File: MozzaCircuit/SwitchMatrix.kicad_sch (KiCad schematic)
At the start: 94 parts, among them SW13 SW_ChocV2_rev, SW14 SW_ChocV2_rev, SW15 SW_ChocV2_rev, SW21 SW_ChocV2_rev, SW22 SW_ChocV2_rev, SW23 SW_ChocV2_rev, SW24 SW_ChocV2_rev, SW25 SW_ChocV2_rev, SW31 SW_ChocV2_rev, SW32 SW_ChocV2_rev, SW33 SW_ChocV2_rev, SW34 SW_ChocV2_rev, SW35 SW_ChocV2_rev, SW41 SW_ChocV2_rev, SW42 SW_ChocV2_rev, SW43 SW_ChocV2_rev, SW44 SW_ChocV2_rev, SW51 SW_ChocV2_rev, SW52 SW_ChocV2_rev, SW53 SW_ChocV2_rev, SW54 SW_ChocV2_rev, SW61 SW_ChocV2_rev, SW62 SW_ChocV2_rev, SW63 SW_ChocV2_rev, SW64 SW_ChocV2_rev, SW71 SW_ChocV2_rev, SW72 SW_ChocV2_rev, SW73 SW_ChocV2_rev, SW82 SW_ChocV2_rev, SW83 SW_ChocV2_rev, SW84 SW_ChocV2_rev

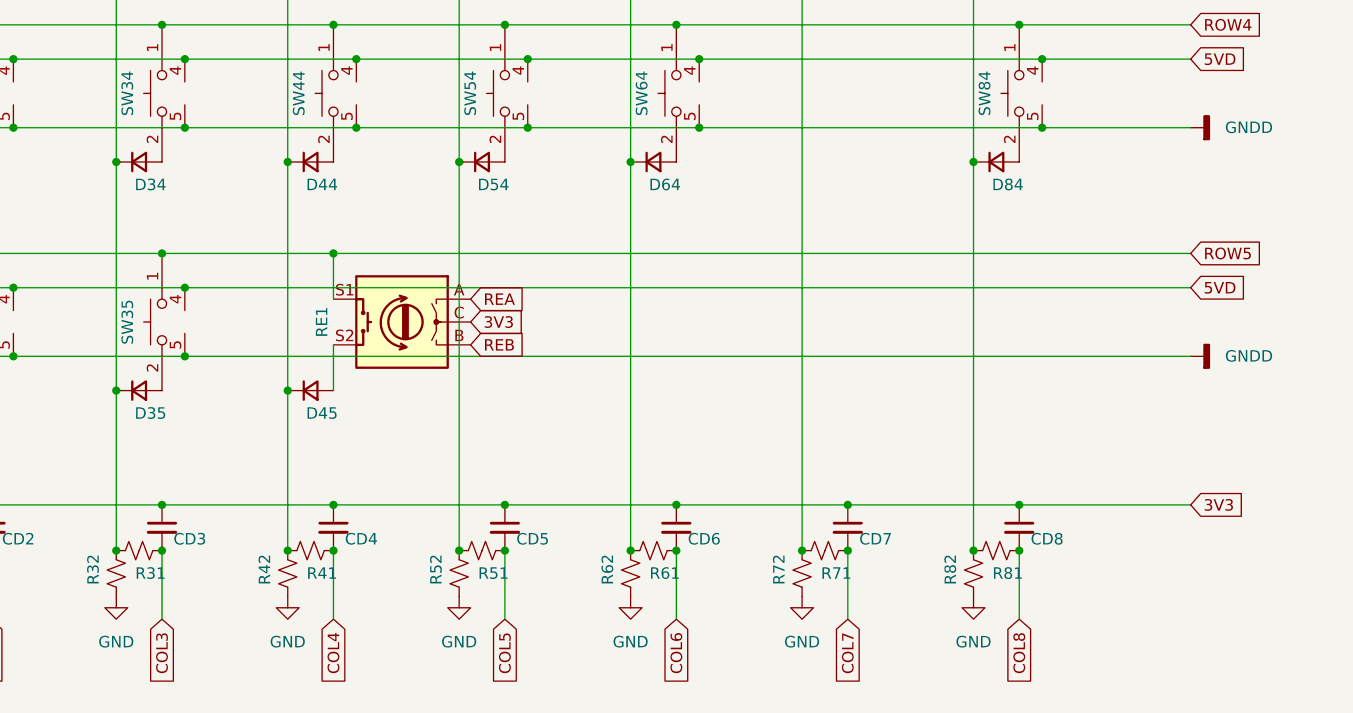
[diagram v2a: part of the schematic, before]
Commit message: rotate rot_enc
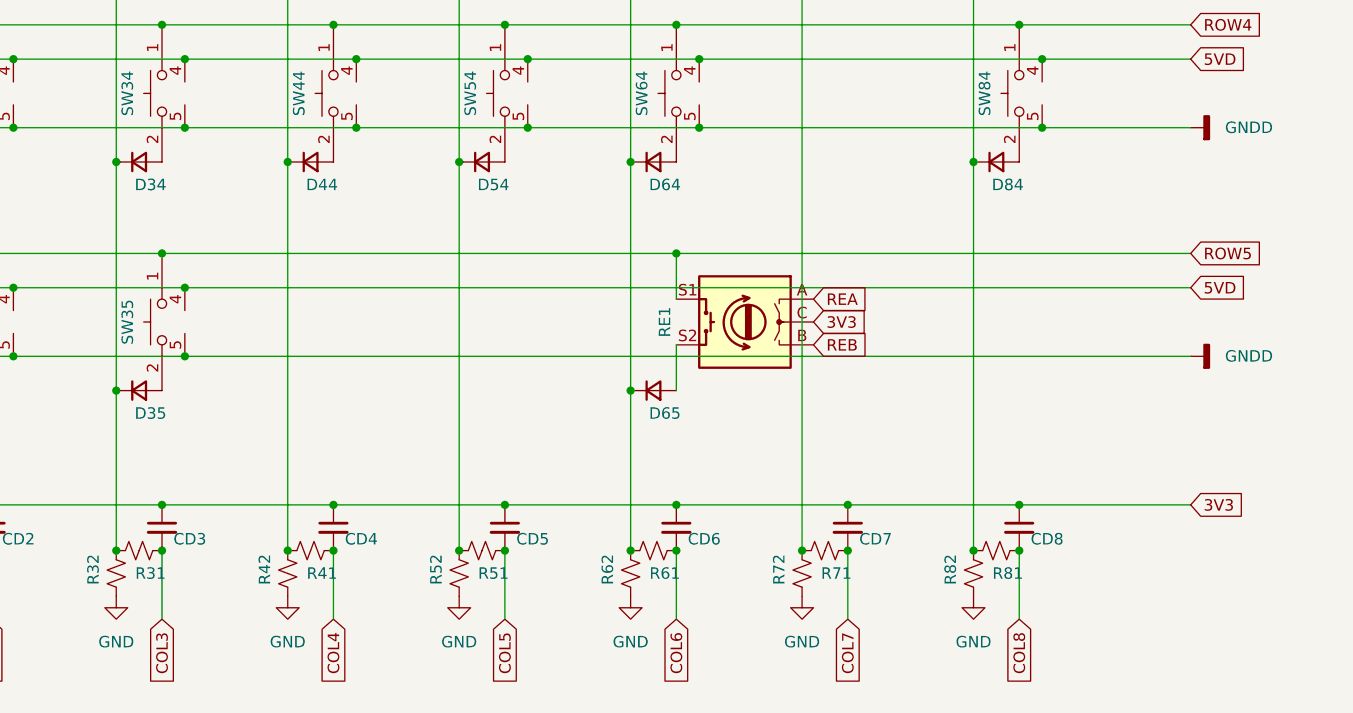
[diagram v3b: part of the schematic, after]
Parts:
- renumbered D45 to D65
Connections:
- net at D41.1 (K), D42.1 (K), D43.1 (K)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: no longer D65.1 (K)
- net at D61.1 (K), D62.1 (K), D63.1 (K)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: now also D65.1 (K)
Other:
- moved on the sheet: D65, RE1
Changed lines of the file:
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@@
   (junction (at 72.39 113.03) (diameter 0) (color 0 0 0 0)
   )
-  (junction (at 88.9 127) (diameter 0) (color 0 0 0 0)
-  )
   (junction (at 69.85 76.2) (diameter 0) (color 0 0 0 0)
   )
@@
   (junction (at 50.8 101.6) (diameter 0) (color 0 0 0 0)
   )
+  (junction (at 121.92 142.24) (diameter 0) (color 0 0 0 0)
+  )
   (junction (at 72.39 54.61) (diameter 0) (color 0 0 0 0)
   )
@@
   (junction (at 53.34 80.01) (diameter 0) (color 0 0 0 0)
   )
+  (junction (at 127 127) (diameter 0) (color 0 0 0 0)
+  )
   (junction (at 53.34 87.63) (diameter 0) (color 0 0 0 0)
   )
@@
   (junction (at 88.9 25.4) (diameter 0) (color 0 0 0 0)
   )
-  (junction (at 83.82 142.24) (diameter 0) (color 0 0 0 0)
-  )
   (junction (at 148.59 62.23) (diameter 0) (color 0 0 0 0)
   )
@@
     (stroke (width 0) (type default) (color 0 0 0 0))
   )
-  (wire (pts (xy 83.82 116.84) (xy 83.82 142.24))
-    (stroke (width 0) (type default) (color 0 0 0 0))
-  )
   (wire (pts (xy 148.59 54.61) (xy 167.64 54.61))
     (stroke (width 0) (type default) (color 0 0 0 0))
@@
     (stroke (width 0) (type default) (color 0 0 0 0))
   )
-  (wire (pts (xy 88.9 137.16) (xy 88.9 142.24))
+  (wire (pts (xy 127 137.16) (xy 127 142.24))
     (stroke (width 0) (type default) (color 0 0 0 0))
   )
@@
     (stroke (width 0) (type default) (color 0 0 0 0))
   )
-  (wire (pts (xy 88.9 127) (xy 184.15 127))
-    (stroke (width 0) (type default) (color 0 0 0 0))
-  )
   (wire (pts (xy 72.39 80.01) (xy 91.44 80.01))
     (stroke (width 0) (type default) (color 0 0 0 0))
@@
     (stroke (width 0) (type default) (color 0 0 0 0))
   )
-  (wire (pts (xy 83.82 142.24) (xy 83.82 160.02))
+  (wire (pts (xy 83.82 116.84) (xy 83.82 160.02))
     (stroke (width 0) (type default) (color 0 0 0 0))
   )
@@
     (stroke (width 0) (type default) (color 0 0 0 0))
   )
+  (wire (pts (xy 127 127) (xy 184.15 127))
+    (stroke (width 0) (type default) (color 0 0 0 0))
+  )
   (wire (pts (xy 140.97 66.04) (xy 140.97 91.44))
     (stroke (width 0) (type default) (color 0 0 0 0))
@@
     (stroke (width 0) (type default) (color 0 0 0 0))
   )
+  (wire (pts (xy 121.92 142.24) (xy 121.92 160.02))
+    (stroke (width 0) (type default) (color 0 0 0 0))
+  )
   (wire (pts (xy 146.05 154.94) (xy 165.1 154.94))
     (stroke (width 0) (type default) (color 0 0 0 0))
@@
     (stroke (width 0) (type default) (color 0 0 0 0))
   )
-  (wire (pts (xy 121.92 116.84) (xy 121.92 160.02))
+  (wire (pts (xy 121.92 116.84) (xy 121.92 142.24))
     (stroke (width 0) (type default) (color 0 0 0 0))
   )
@@
     (stroke (width 0) (type default) (color 0 0 0 0))
   )
-  (wire (pts (xy 88.9 127) (xy 88.9 132.08))
+  (wire (pts (xy 127 127) (xy 127 132.08))
     (stroke (width 0) (type default) (color 0 0 0 0))
   )
@@
     (stroke (width 0) (type default) (color 0 0 0 0))
   )
-  (wire (pts (xy 69.85 127) (xy 88.9 127))
+  (wire (pts (xy 69.85 127) (xy 127 127))
     (stroke (width 0) (type default) (color 0 0 0 0))
   )
@@
     )
   )
-  (global_label "3V3" (shape input) (at 104.14 134.62 0) (fields_autoplaced)
+  (global_label "3V3" (shape input) (at 142.24 134.62 0) (fields_autoplaced)
     (effects (font (size 1.27 1.27)) (justify left))
-    (property "Intersheet References" "${INTERSHEET_REFS}" (id 0) (at 110.0607 134.5406 0)
-      (effects (font (size 1.27 1.27)) (justify left) hide)
-    )
-  )
-  (global_label "REA" (shape input) (at 104.14 132.08 0) (fields_autoplaced)
+    (property "Intersheet References" "${INTERSHEET_REFS}" (id 0) (at 148.1607 134.5406 0)
+      (effects (font (size 1.27 1.27)) (justify left) hide)
+    )
+  )
+  (global_label "REA" (shape input) (at 142.24 132.08 0) (fields_autoplaced)
     (effects (font (size 1.27 1.27)) (justify left))
-    (property "Intersheet References" "${INTERSHEET_REFS}" (id 0) (at 110.0607 132.0006 0)
+    (property "Intersheet References" "${INTERSHEET_REFS}" (id 0) (at 148.1607 132.0006 0)
       (effects (font (size 1.27 1.27)) (justify left) hide)
     )
@@
     )
   )
-  (global_label "REB" (shape input) (at 104.14 137.16 0) (fields_autoplaced)
+  (global_label "REB" (shape input) (at 142.24 137.16 0) (fields_autoplaced)
     (effects (font (size 1.27 1.27)) (justify left))
-    (property "Intersheet References" "${INTERSHEET_REFS}" (id 0) (at 110.2421 137.0806 0)
+    (property "Intersheet References" "${INTERSHEET_REFS}" (id 0) (at 148.3421 137.0806 0)
       (effects (font (size 1.27 1.27)) (justify left) hide)
     )
@@
     (pin "1")
   )
-  (symbol (lib_id "Device:RotaryEncoder_Switch") (at 96.52 134.62 0) (mirror y) (unit 1)
-    (in_bom yes) (on_board yes)
-    (property "Reference" "RE1" (id 0) (at 87.63 134.62 90))
-    (property "Value" "RotaryEncoder_Switch" (id 1) (at 96.52 127 0)
-      (effects (font (size 1.27 1.27)) hide)
-    )
-    (property "Footprint" "00_KeyParts:RotaryEncoder_Bourns_PEC12R-4215F" (id 2) (at 100.33 130.556 0)
-      (effects (font (size 1.27 1.27)) hide)
-    )
-    (property "Datasheet" "~" (id 3) (at 96.52 128.016 0)
+  (symbol (lib_id "Device:RotaryEncoder_Switch") (at 134.62 134.62 0) (mirror y) (unit 1)
+    (in_bom yes) (on_board yes)
+    (property "Reference" "RE1" (id 0) (at 125.73 134.62 90))
+    (property "Value" "RotaryEncoder_Switch" (id 1) (at 134.62 127 0)
+      (effects (font (size 1.27 1.27)) hide)
+    )
+    (property "Footprint" "00_KeyParts:RotaryEncoder_Bourns_PEC12R-4215F" (id 2) (at 138.43 130.556 0)
+      (effects (font (size 1.27 1.27)) hide)
+    )
+    (property "Datasheet" "~" (id 3) (at 134.62 128.016 0)
       (effects (font (size 1.27 1.27)) hide)
     )
@@
     (pin "2")
   )
-  (symbol (lib_id "Device:D_Small") (at 86.36 142.24 0) (unit 1)
-    (in_bom yes) (on_board yes)
-    (property "Reference" "D45" (id 0) (at 87.63 144.78 0))
-    (property "Value" "D_Small" (id 1) (at 86.36 138.43 0)
-      (effects (font (size 1.27 1.27)) hide)
-    )
-    (property "Footprint" "00_KeyParts:D_SOD-323_both_sides" (id 2) (at 86.36 142.24 90)
-      (effects (font (size 1.27 1.27)) hide)
-    )
-    (property "Datasheet" "~" (id 3) (at 86.36 142.24 90)
-      (effects (font (size 1.27 1.27)) hide)
-    )
+  (symbol (lib_id "Device:D_Small") (at 124.46 142.24 0) (unit 1)
+    (in_bom yes) (on_board yes)
+    (property "Reference" "D65" (id 0) (at 125.73 144.78 0))
+    (property "Value" "D_Small" (id 1) (at 124.46 138.43 0)
+      (effects (font (size 1.27 1.27)) hide)
+    )
+    (property "Footprint" "00_KeyParts:D_SOD-323_both_sides" (id 2) (at 124.46 142.24 90)
+      (effects (font (size 1.27 1.27)) hide)
+    )
+    (property "Datasheet" "~" (id 3) (at 124.46 142.24 90)
+      (effects (font (size 1.27 1.27)) hide)
+    )

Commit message: rotenc diode
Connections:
- net ROW5: now also RE1.S2; no longer RE1.S1
- net at D65.2 (A): now also RE1.S1; no longer RE1.S2
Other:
- moved on the sheet: RE1
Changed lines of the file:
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@@
     )
   )
-  (global_label "REA" (shape input) (at 142.24 132.08 0) (fields_autoplaced)
-    (effects (font (size 1.27 1.27)) (justify left))
-    (property "Intersheet References" "${INTERSHEET_REFS}" (id 0) (at 148.1607 132.0006 0)
+  (global_label "REA" (shape input) (at 142.24 137.16 0) (fields_autoplaced)
+    (effects (font (size 1.27 1.27)) (justify left))
+    (property "Intersheet References" "${INTERSHEET_REFS}" (id 0) (at 148.1607 137.0806 0)
       (effects (font (size 1.27 1.27)) (justify left) hide)
     )
@@
     )
   )
-  (global_label "REB" (shape input) (at 142.24 137.16 0) (fields_autoplaced)
-    (effects (font (size 1.27 1.27)) (justify left))
-    (property "Intersheet References" "${INTERSHEET_REFS}" (id 0) (at 148.3421 137.0806 0)
+  (global_label "REB" (shape input) (at 142.24 132.08 0) (fields_autoplaced)
+    (effects (font (size 1.27 1.27)) (justify left))
+    (property "Intersheet References" "${INTERSHEET_REFS}" (id 0) (at 148.3421 132.0006 0)
       (effects (font (size 1.27 1.27)) (justify left) hide)
     )
@@
     (pin "1")
   )
-  (symbol (lib_id "Device:RotaryEncoder_Switch") (at 134.62 134.62 0) (mirror y) (unit 1)
+  (symbol (lib_id "Device:RotaryEncoder_Switch") (at 134.62 134.62 180) (unit 1)
     (in_bom yes) (on_board yes)
     (property "Reference" "RE1" (id 0) (at 125.73 134.62 90))
-    (property "Value" "RotaryEncoder_Switch" (id 1) (at 134.62 127 0)
-      (effects (font (size 1.27 1.27)) hide)
-    )
-    (property "Footprint" "00_KeyParts:RotaryEncoder_Bourns_PEC12R-4215F" (id 2) (at 138.43 130.556 0)
-      (effects (font (size 1.27 1.27)) hide)
-    )
-    (property "Datasheet" "~" (id 3) (at 134.62 128.016 0)
-      (effects (font (size 1.27 1.27)) hide)
-    )
+    (property "Value" "RotaryEncoder_Switch" (id 1) (at 134.62 142.24 0)
+      (effects (font (size 1.27 1.27)) hide)
+    )
+    (property "Footprint" "00_KeyParts:RotaryEncoder_Bourns_PEC12R-4215F" (id 2) (at 138.43 138.684 0)
+      (effects (font (size 1.27 1.27)) hide)
+    )
+    (property "Datasheet" "~" (id 3) (at 134.62 141.224 0)
+      (effects (font (size 1.27 1.27)) hide)
+    )

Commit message: led lines
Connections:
- net 5VD: now also SW25.5; no longer SW25.4
- net GNDD: now also SW25.4; no longer SW25.5
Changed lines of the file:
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@@
   (junction (at 160.02 91.44) (diameter 0) (color 0 0 0 0)
   )
-  (junction (at 72.39 138.43) (diameter 0) (color 0 0 0 0)
-  )
   (junction (at 50.8 76.2) (diameter 0) (color 0 0 0 0)
   )
@@
   (junction (at 234.95 138.43) (diameter 0) (color 0 0 0 0)
   )
-  (junction (at 72.39 130.81) (diameter 0) (color 0 0 0 0)
-  )
   (junction (at 129.54 113.03) (diameter 0) (color 0 0 0 0)
   )
@@
   (junction (at 91.44 80.01) (diameter 0) (color 0 0 0 0)
   )
-  (junction (at 53.34 130.81) (diameter 0) (color 0 0 0 0)
-  )
   (junction (at 88.9 160.02) (diameter 0) (color 0 0 0 0)
   )
@@
   (junction (at 64.77 116.84) (diameter 0) (color 0 0 0 0)
   )
-  (junction (at 53.34 138.43) (diameter 0) (color 0 0 0 0)
-  )
   (junction (at 146.05 160.02) (diameter 0) (color 0 0 0 0)
   )
@@
     (stroke (width 0) (type default) (color 0 0 0 0))
   )
-  (wire (pts (xy 34.29 130.81) (xy 53.34 130.81))
-    (stroke (width 0) (type default) (color 0 0 0 0))
-  )
   (wire (pts (xy 110.49 80.01) (xy 129.54 80.01))
     (stroke (width 0) (type default) (color 0 0 0 0))
@@
     (stroke (width 0) (type default) (color 0 0 0 0))
   )
-  (wire (pts (xy 72.39 130.81) (xy 184.15 130.81))
-    (stroke (width 0) (type default) (color 0 0 0 0))
-  )
   (wire (pts (xy 229.87 127) (xy 229.87 138.43))
     (stroke (width 0) (type default) (color 0 0 0 0))
@@
     (stroke (width 0) (type default) (color 0 0 0 0))
   )
-  (wire (pts (xy 34.29 138.43) (xy 53.34 138.43))
-    (stroke (width 0) (type default) (color 0 0 0 0))
-  )
   (wire (pts (xy 165.1 154.94) (xy 184.15 154.94))
     (stroke (width 0) (type default) (color 0 0 0 0))
@@
     (stroke (width 0) (type default) (color 0 0 0 0))
   )
-  (wire (pts (xy 53.34 138.43) (xy 72.39 138.43))
-    (stroke (width 0) (type default) (color 0 0 0 0))
-  )
   (wire (pts (xy 53.34 105.41) (xy 72.39 105.41))
     (stroke (width 0) (type default) (color 0 0 0 0))
@@
   )
   (wire (pts (xy 129.54 105.41) (xy 167.64 105.41))
-    (stroke (width 0) (type default) (color 0 0 0 0))
-  )
-  (wire (pts (xy 72.39 138.43) (xy 184.15 138.43))
-    (stroke (width 0) (type default) (color 0 0 0 0))
-  )
-  (wire (pts (xy 53.34 130.81) (xy 72.39 130.81))
     (stroke (width 0) (type default) (color 0 0 0 0))
   )
@@
     )
   )
+  (global_label "5VD" (shape input) (at 53.34 138.43 0) (fields_autoplaced)
+    (effects (font (size 1.27 1.27)) (justify left))
+    (property "Intersheet References" "${INTERSHEET_REFS}" (id 0) (at 59.3212 138.3506 0)
+      (effects (font (size 1.27 1.27)) (justify left) hide)
+    )
+  )
   (global_label "COL7" (shape input) (at 146.05 167.64 270) (fields_autoplaced)
     (effects (font (size 1.27 1.27)) (justify right))
@@
     )
   )
+  (global_label "5VD" (shape input) (at 34.29 130.81 0) (fields_autoplaced)
+    (effects (font (size 1.27 1.27)) (justify left))
+    (property "Intersheet References" "${INTERSHEET_REFS}" (id 0) (at 40.2712 130.7306 0)
+      (effects (font (size 1.27 1.27)) (justify left) hide)
+    )
+  )
   (global_label "COL2" (shape input) (at 50.8 167.64 270) (fields_autoplaced)
     (effects (font (size 1.27 1.27)) (justify right))
@@
     )
   )
-  (global_label "5VD" (shape input) (at 184.15 130.81 0) (fields_autoplaced)
+  (global_label "5VD" (shape input) (at 72.39 130.81 0) (fields_autoplaced)
     (effects (font (size 1.27 1.27)) (justify left))
-    (property "Intersheet References" "${INTERSHEET_REFS}" (id 0) (at 190.1312 130.7306 0)
+    (property "Intersheet References" "${INTERSHEET_REFS}" (id 0) (at 78.3712 130.7306 0)
       (effects (font (size 1.27 1.27)) (justify left) hide)
     )
@@
     (pin "2")
   )
+  (symbol (lib_id "power:GNDD") (at 53.34 130.81 90) (unit 1)
+    (in_bom yes) (on_board yes) (fields_autoplaced)
+    (property "Reference" "#PWR0139" (id 0) (at 59.69 130.81 0)
+      (effects (font (size 1.27 1.27)) hide)
+    )
+    (property "Value" "GNDD" (id 1) (at 57.15 130.8099 90)
+      (effects (font (size 1.27 1.27)) (justify right))
+    )
+    (property "Footprint" "" (id 2) (at 53.34 130.81 0)
+      (effects (font (size 1.27 1.27)) hide)
+    )
+    (property "Datasheet" "" (id 3) (at 53.34 130.81 0)
+      (effects (font (size 1.27 1.27)) hide)
+    )
+    (pin "1")
+  )
   (symbol (lib_id "Device:D_Small") (at 86.36 40.64 0) (unit 1)
     (in_bom yes) (on_board yes)
@@
     (pin "1")
   )
-  (symbol (lib_id "power:GNDD") (at 184.15 138.43 90) (unit 1)
+  (symbol (lib_id "power:GNDD") (at 72.39 138.43 90) (unit 1)
     (in_bom yes) (on_board yes) (fields_autoplaced)
-    (property "Reference" "#PWR0124" (id 0) (at 190.5 138.43 0)
-      (effects (font (size 1.27 1.27)) hide)
-    )
-    (property "Value" "GNDD" (id 1) (at 187.96 138.4299 90)
+    (property "Reference" "#PWR0124" (id 0) (at 78.74 138.43 0)
+      (effects (font (size 1.27 1.27)) hide)
+    )
+    (property "Value" "GNDD" (id 1) (at 76.2 138.4299 90)
       (effects (font (size 1.27 1.27)) (justify right))
     )
-    (property "Footprint" "" (id 2) (at 184.15 138.43 0)
-      (effects (font (size 1.27 1.27)) hide)
-    )
-    (property "Datasheet" "" (id 3) (at 184.15 138.43 0)
+    (property "Footprint" "" (id 2) (at 72.39 138.43 0)
+      (effects (font (size 1.27 1.27)) hide)
+    )
+    (property "Datasheet" "" (id 3) (at 72.39 138.43 0)
       (effects (font (size 1.27 1.27)) hide)
     )
@@
     (pin "2")
   )
+  (symbol (lib_id "power:GNDD") (at 34.29 138.43 90) (unit 1)
+    (in_bom yes) (on_board yes) (fields_autoplaced)
+    (property "Reference" "#PWR0138" (id 0) (at 40.64 138.43 0)
+      (effects (font (size 1.27 1.27)) hide)
+    )
+    (property "Value" "GNDD" (id 1) (at 38.1 138.4299 90)
+      (effects (font (size 1.27 1.27)) (justify right))
+    )
+    (property "Footprint" "" (id 2) (at 34.29 138.43 0)
+      (effects (font (size 1.27 1.27)) hide)
+    )
+    (property "Datasheet" "" (id 3) (at 34.29 138.43 0)
+      (effects (font (size 1.27 1.27)) hide)
+    )
+    (pin "1")
+  )
   (symbol (lib_id "power:GND") (at 229.87 143.51 0) (unit 1)
